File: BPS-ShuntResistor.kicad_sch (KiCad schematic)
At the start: 18 parts, among them J3 Amp_Conn

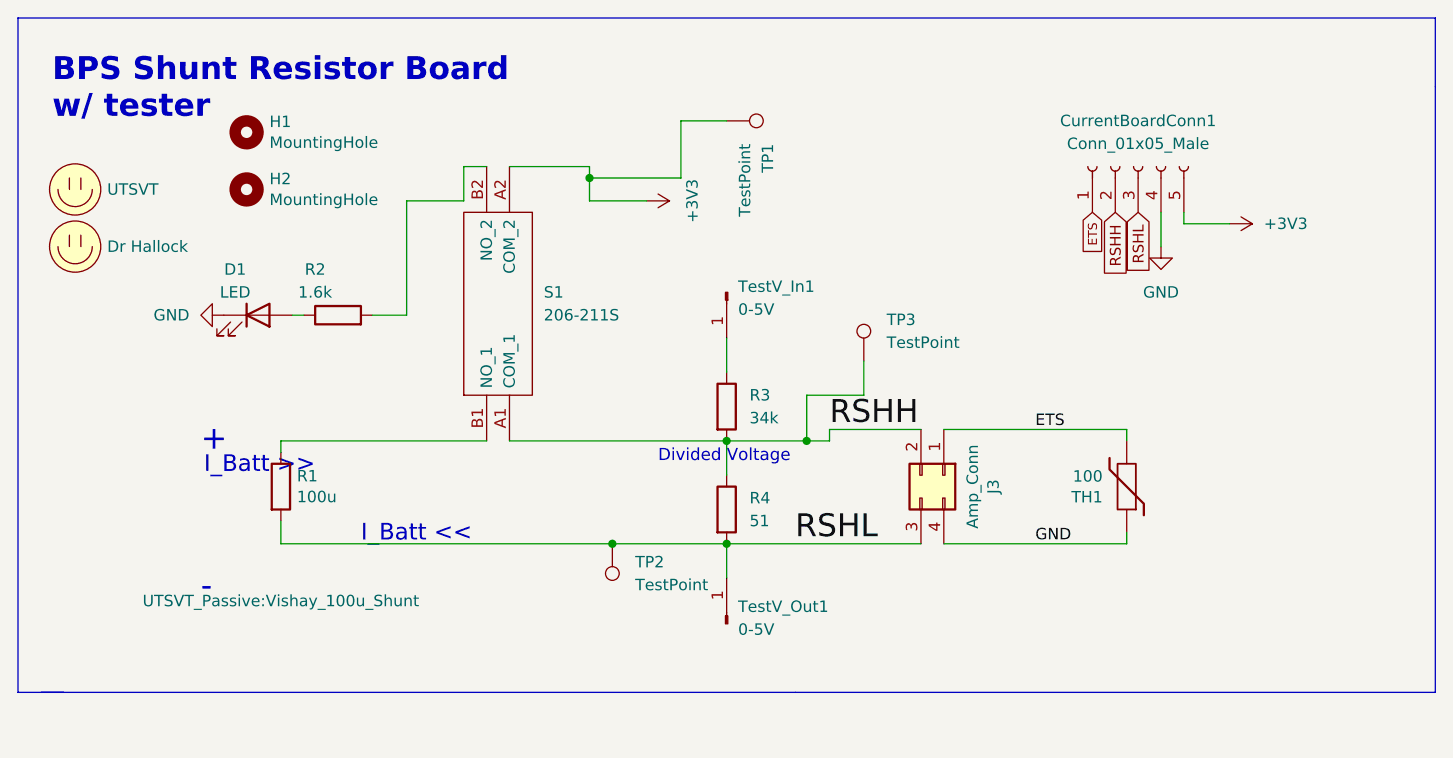
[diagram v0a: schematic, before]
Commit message: reorganizing board
workign on sync between amp board and this one
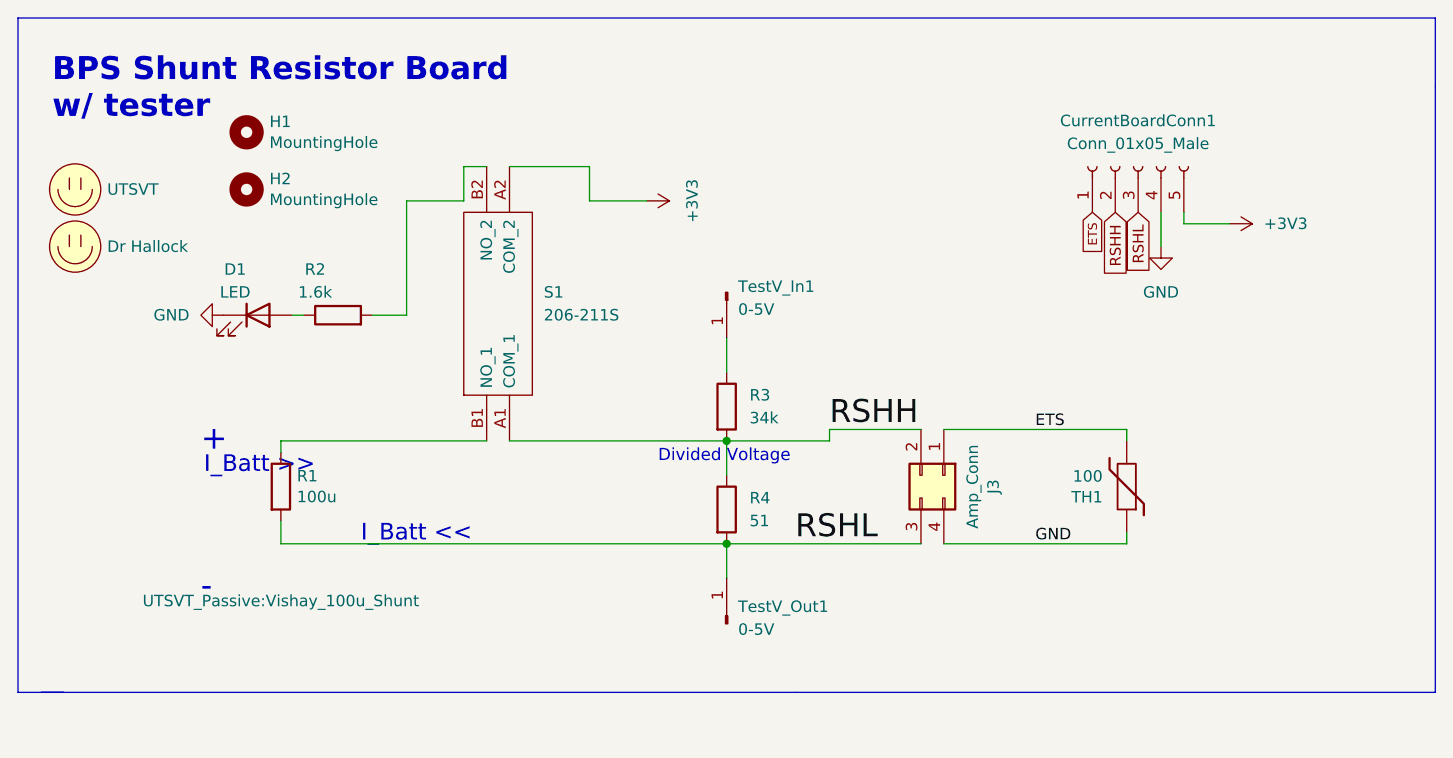
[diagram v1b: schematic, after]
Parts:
- removed TP1, TP2, TP3: TestPoint, TestPoint:TestPoint_Keystone_5005-5009_Compact, symbol Connector:TestPoint
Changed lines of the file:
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@@
 (kicad_sch (version 20211123) (generator eeschema)
   (paper "A4")
-  (junction (at 140.97 118.11) (diameter 0) (color 0 0 0 0)
-  )
-  (junction (at 162.56 106.68) (diameter 0) (color 0 0 0 0)
-  )
-  (junction (at 138.43 77.47) (diameter 0) (color 0 0 0 0)
-  )
   (junction (at 153.67 106.68) (diameter 0) (color 0 0 0 0)
   )
@@
     (stroke (width 0) (type default) (color 0 0 0 0))
   )
-  (wire (pts (xy 153.67 106.68) (xy 162.56 106.68))
-    (stroke (width 0) (type default) (color 0 0 0 0))
-  )
-  (wire (pts (xy 140.97 118.11) (xy 153.67 118.11))
+  (wire (pts (xy 153.67 106.68) (xy 165.1 106.68))
     (stroke (width 0) (type default) (color 0 0 0 0))
   )
@@
     (stroke (width 0) (type default) (color 0 0 0 0))
   )
-  (wire (pts (xy 162.56 101.6) (xy 162.56 106.68))
-    (stroke (width 0) (type default) (color 0 0 0 0))
-  )
   (wire (pts (xy 104.14 106.68) (xy 104.14 107.95))
     (stroke (width 0) (type default) (color 0 0 0 0))
@@
     (stroke (width 0) (type default) (color 0 0 0 0))
   )
-  (wire (pts (xy 148.59 71.12) (xy 148.59 77.47))
-    (stroke (width 0) (type default) (color 0 0 0 0))
-  )
   (wire (pts (xy 153.67 118.11) (xy 153.67 121.92))
     (stroke (width 0) (type default) (color 0 0 0 0))
   )
-  (wire (pts (xy 148.59 77.47) (xy 138.43 77.47))
-    (stroke (width 0) (type default) (color 0 0 0 0))
-  )
   (wire (pts (xy 124.46 80.01) (xy 124.46 76.2))
     (stroke (width 0) (type default) (color 0 0 0 0))
@@
     (stroke (width 0) (type default) (color 0 0 0 0))
   )
-  (wire (pts (xy 138.43 77.47) (xy 138.43 80.01))
+  (wire (pts (xy 138.43 76.2) (xy 138.43 80.01))
     (stroke (width 0) (type default) (color 0 0 0 0))
   )
@@
     (stroke (width 0) (type default) (color 0 0 0 0))
   )
-  (wire (pts (xy 153.67 71.12) (xy 148.59 71.12))
-    (stroke (width 0) (type default) (color 0 0 0 0))
-  )
-  (wire (pts (xy 168.91 101.6) (xy 162.56 101.6))
-    (stroke (width 0) (type default) (color 0 0 0 0))
-  )
   (wire (pts (xy 114.3 92.71) (xy 118.11 92.71))
     (stroke (width 0) (type default) (color 0 0 0 0))
   )
-  (wire (pts (xy 104.14 118.11) (xy 140.97 118.11))
+  (wire (pts (xy 104.14 118.11) (xy 153.67 118.11))
     (stroke (width 0) (type default) (color 0 0 0 0))
   )
@@
     (stroke (width 0) (type default) (color 0 0 0 0))
   )
-  (wire (pts (xy 138.43 76.2) (xy 138.43 77.47))
-    (stroke (width 0) (type default) (color 0 0 0 0))
-  )
   (wire (pts (xy 105.41 92.71) (xy 106.68 92.71))
     (stroke (width 0) (type default) (color 0 0 0 0))
   )
   (wire (pts (xy 153.67 106.68) (xy 153.67 110.49))
-    (stroke (width 0) (type default) (color 0 0 0 0))
-  )
-  (wire (pts (xy 168.91 97.79) (xy 168.91 101.6))
-    (stroke (width 0) (type default) (color 0 0 0 0))
-  )
-  (wire (pts (xy 162.56 106.68) (xy 165.1 106.68))
     (stroke (width 0) (type default) (color 0 0 0 0))
   )
@@
     (pin "1")
   )
-  (symbol (lib_id "Connector:TestPoint") (at 168.91 97.79 0) (unit 1)
-    (in_bom yes) (on_board yes) (fields_autoplaced)
-    (property "Reference" "TP3" (id 0) (at 171.45 93.2179 0)
-      (effects (font (size 1.27 1.27)) (justify left))
-    )
-    (property "Value" "TestPoint" (id 1) (at 171.45 95.7579 0)
-      (effects (font (size 1.27 1.27)) (justify left))
-    )
-    (property "Footprint" "TestPoint:TestPoint_Keystone_5005-5009_Compact" (id 2) (at 173.99 97.79 0)
-      (effects (font (size 1.27 1.27)) hide)
-    )
-    (property "Datasheet" "~" (id 3) (at 173.99 97.79 0)
-      (effects (font (size 1.27 1.27)) hide)
-    )
-    (pin "1")
-  )
   (symbol (lib_id "Connector:Conn_01x01_Male") (at 153.67 90.17 270) (unit 1)
     (in_bom yes) (on_board yes) (fields_autoplaced)
@@
     )
     (property "Datasheet" "" (id 3) (at 209.55 82.55 0)
-      (effects (font (size 1.27 1.27)) hide)
-    )
-    (pin "1")
-  )
-  (symbol (lib_id "Connector:TestPoint") (at 153.67 71.12 270) (unit 1)
-    (in_bom yes) (on_board yes) (fields_autoplaced)
-    (property "Reference" "TP1" (id 0) (at 158.2421 73.66 0)
-      (effects (font (size 1.27 1.27)) (justify left))
-    )
-    (property "Value" "TestPoint" (id 1) (at 155.7021 73.66 0)
-      (effects (font (size 1.27 1.27)) (justify left))
-    )
-    (property "Footprint" "TestPoint:TestPoint_Keystone_5005-5009_Compact" (id 2) (at 153.67 76.2 0)
-      (effects (font (size 1.27 1.27)) hide)
-    )
-    (property "Datasheet" "~" (id 3) (at 153.67 76.2 0)
-      (effects (font (size 1.27 1.27)) hide)
-    )
-    (pin "1")
-  )
-  (symbol (lib_id "Connector:TestPoint") (at 140.97 118.11 180) (unit 1)
-    (in_bom yes) (on_board yes) (fields_autoplaced)
-    (property "Reference" "TP2" (id 0) (at 143.51 120.1419 0)
-      (effects (font (size 1.27 1.27)) (justify right))
-    )
-    (property "Value" "TestPoint" (id 1) (at 143.51 122.6819 0)
-      (effects (font (size 1.27 1.27)) (justify right))
-    )
-    (property "Footprint" "TestPoint:TestPoint_Keystone_5005-5009_Compact" (id 2) (at 135.89 118.11 0)
-      (effects (font (size 1.27 1.27)) hide)
-    )
-    (property "Datasheet" "~" (id 3) (at 135.89 118.11 0)
       (effects (font (size 1.27 1.27)) hide)
     )
@@
       (reference "TH1") (unit 1) (value "100") (footprint "Resistor_SMD:R_0805_2012Metric")
     )
-    (path "/a2c0827d-27e7-459e-b74e-82b71d0bcf7d"
-      (reference "TP1") (unit 1) (value "TestPoint") (footprint "TestPoint:TestPoint_Keystone_5005-5009_Compact")
-    )
-    (path "/a52bbaf7-274f-407b-9c3b-8b7919792ae5"
-      (reference "TP2") (unit 1) (value "TestPoint") (footprint "TestPoint:TestPoint_Keystone_5005-5009_Compact")
-    )
-    (path "/6f9c746a-56ac-4c76-a21a-897a0cead77e"
-      (reference "TP3") (unit 1) (value "TestPoint") (footprint "TestPoint:TestPoint_Keystone_5005-5009_Compact")
-    )
     (path "/84a7fc7b-5bd9-45c8-89b5-3a5bcad31a54"

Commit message: working on rework
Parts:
- removed D1: LED, LED_SMD:LED_0805_2012Metric, symbol Device:LED
- removed R2: 1.6k, Resistor_SMD:R_0805_2012Metric, symbol Device:R
- removed S1: 206-211S, custom footprints:206211S, symbol custom_reqs:206-211S
- removed TestV_In1, TestV_Out1: 0-5V, Connector_PinHeader_2.54mm:PinHeader_1x01_P2.54mm_Vertical, symbol Connector:Conn_01x01_Male
- added ShuntTestJumper: Conn_01x05_Male, Connector_PinHeader_2.54mm:PinHeader_1x05_P2.54mm_Vertical, symbol Connector:Conn_01x05_Female
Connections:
- net RSHH: now also ShuntTestJumper.3 (Pin_3)
- net RSHL: now also ShuntTestJumper.5 (Pin_5)
- net at R1.1: now also ShuntTestJumper.2 (Pin_2)
- net TestIn: now reaches R3.1
- net TestIn: now also ShuntTestJumper.4 (Pin_4)
- no-connect marks 0 -> 1

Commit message: fixing sch
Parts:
- renumbered ShuntTestJumper to ShuntTestJumper1
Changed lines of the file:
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@@
   (symbol (lib_id "Connector:Conn_01x05_Female") (at 128.27 91.44 90) (unit 1)
     (in_bom yes) (on_board yes) (fields_autoplaced)
-    (property "Reference" "ShuntTestJumper" (id 0) (at 128.27 86.36 90))
+    (property "Reference" "ShuntTestJumper1" (id 0) (at 128.27 86.36 90))
     (property "Value" "Conn_01x05_Male" (id 1) (at 128.27 88.9 90))
     (property "Footprint" "Connector_PinHeader_2.54mm:PinHeader_1x05_P2.54mm_Vertical" (id 2) (at 128.27 91.44 0)
@@
     )
     (path "/46651b6a-aae7-4589-85a3-9dbcf0861909"
-      (reference "ShuntTestJumper") (unit 1) (value "Conn_01x05_Male") (footprint "Connector_PinHeader_2.54mm:PinHeader_1x05_P2.54mm_Vertical")
+      (reference "ShuntTestJumper1") (unit 1) (value "Conn_01x05_Male") (footprint "Connector_PinHeader_2.54mm:PinHeader_1x05_P2.54mm_Vertical")
     )
     (path "/bff0be5b-fcea-4d1b-a22e-58c65723f733"

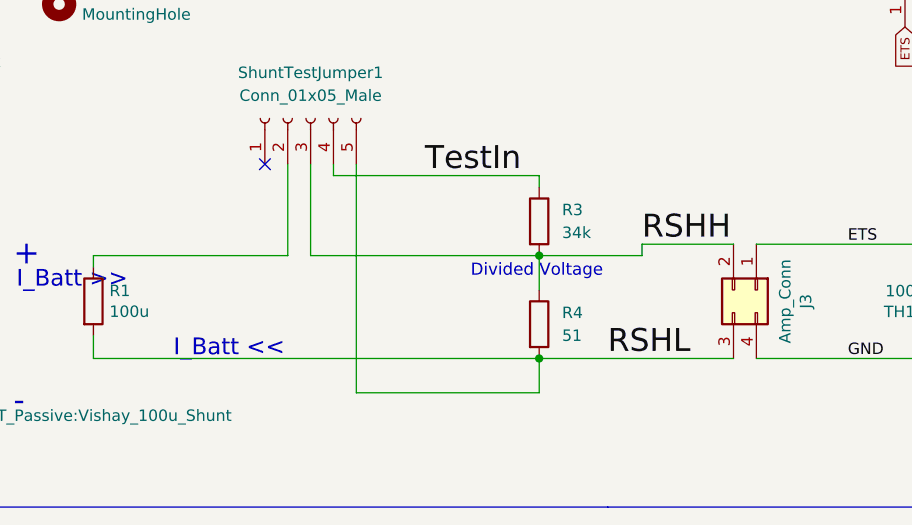
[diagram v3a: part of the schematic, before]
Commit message: Fixed RSHL/RSHH connectors
Net labels were in wrong spot on circuit
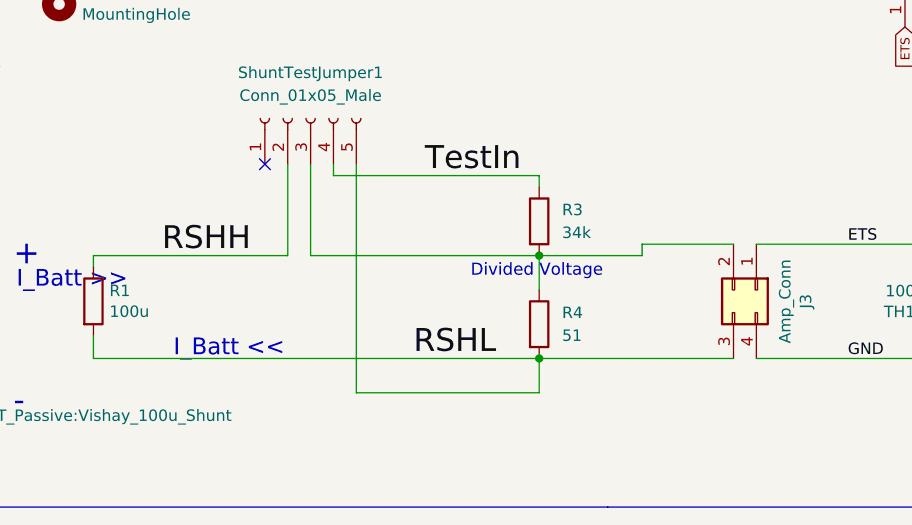
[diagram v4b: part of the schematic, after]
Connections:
- net RSHH: now also R1.1, ShuntTestJumper1.2 (Pin_2); no longer J3.2 (Pin_2), R3.2, R4.1, ShuntTestJumper1.3 (Pin_3)
- new net: J3.2 (Pin_2), R3.2, R4.1, ShuntTestJumper1.3 (Pin_3)
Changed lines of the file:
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@@
     (effects (font (size 1.27 1.27)) (justify left bottom))
   )
-  (label "RSHL" (at 161.29 118.11 0)
+  (label "RSHL" (at 139.7 118.11 0)
     (effects (font (size 2.54 2.54)) (justify left bottom))
   )
@@
     (effects (font (size 1.27 1.27)) (justify left bottom))
   )
-  (label "RSHH" (at 165.1 105.41 0)
+  (label "RSHH" (at 111.76 106.68 0)
     (effects (font (size 2.54 2.54)) (justify left bottom))
   )

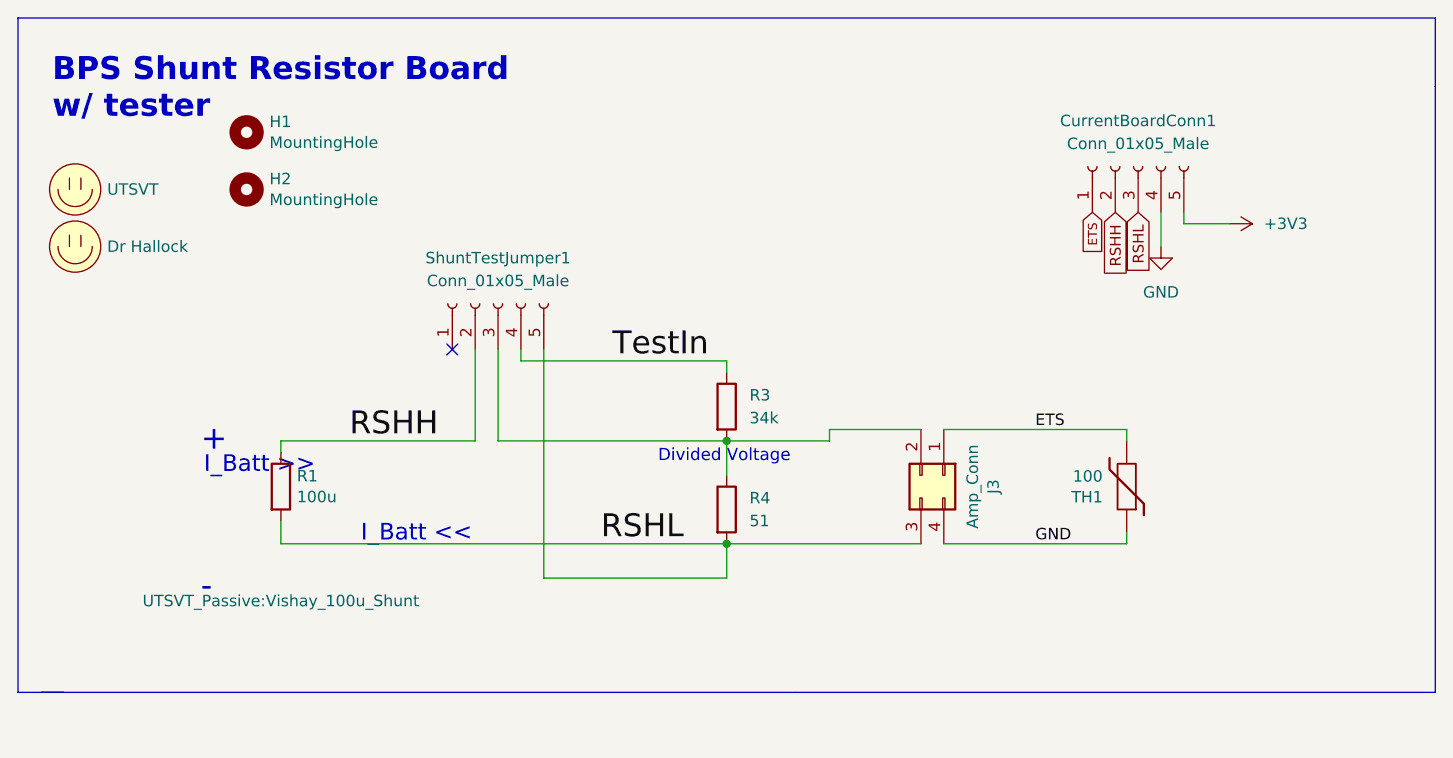
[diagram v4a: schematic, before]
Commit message: moved to exact same positions as tianda
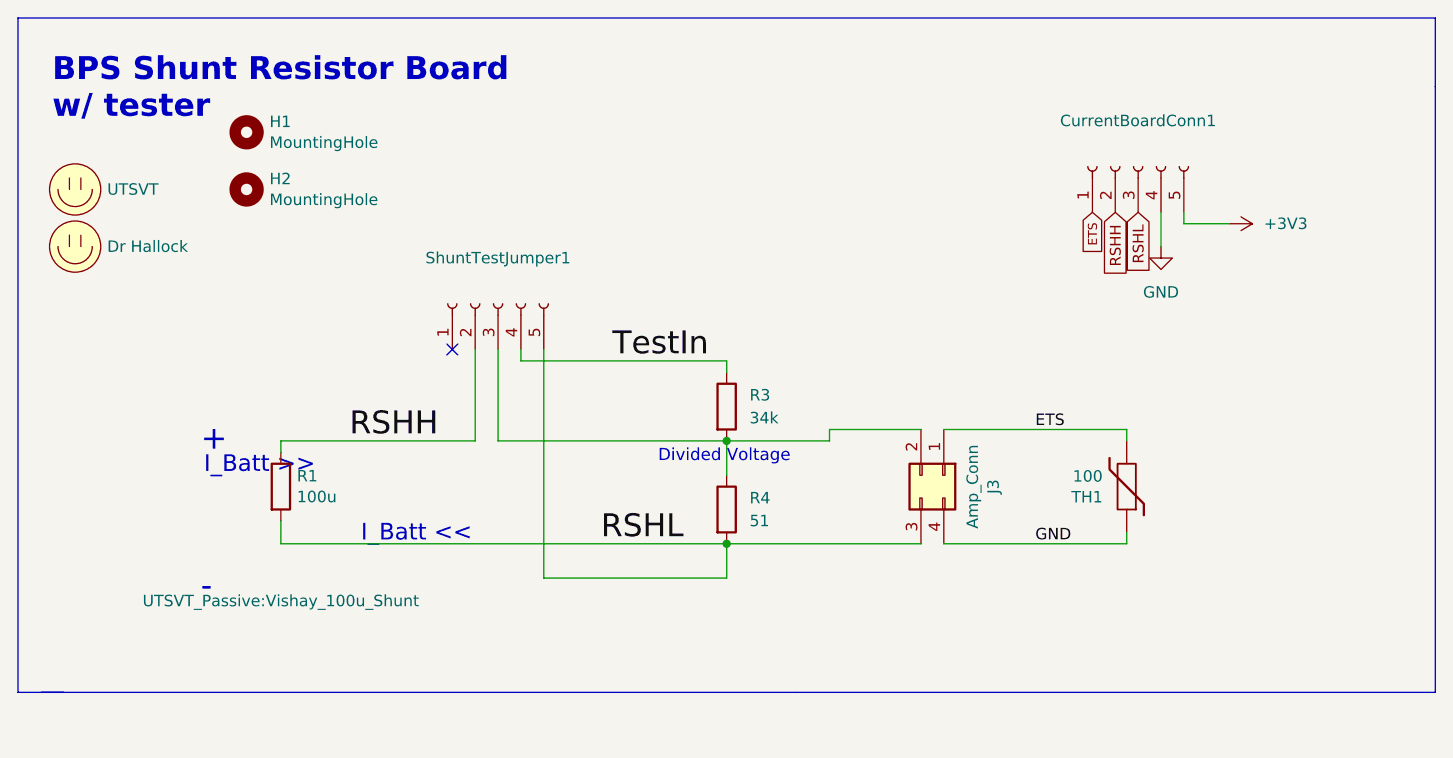
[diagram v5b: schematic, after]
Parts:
- CurrentBoardConn1, ShuntTestJumper1: value Conn_01x05_Male -> (none); footprint Connector_PinHeader_2.54mm:PinHeader_1x05_P2.54mm_Vertical -> (none)
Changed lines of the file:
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@@
     (in_bom yes) (on_board yes) (fields_autoplaced)
     (property "Reference" "ShuntTestJumper1" (id 0) (at 128.27 86.36 90))
-    (property "Value" "Conn_01x05_Male" (id 1) (at 128.27 88.9 90))
-    (property "Footprint" "Connector_PinHeader_2.54mm:PinHeader_1x05_P2.54mm_Vertical" (id 2) (at 128.27 91.44 0)
+    (property "Value" "" (id 1) (at 128.27 88.9 90))
+    (property "Footprint" "" (id 2) (at 128.27 91.44 0)
       (effects (font (size 1.27 1.27)) hide)
     )
@@
     (in_bom yes) (on_board yes) (fields_autoplaced)
     (property "Reference" "CurrentBoardConn1" (id 0) (at 199.39 71.12 90))
-    (property "Value" "Conn_01x05_Male" (id 1) (at 199.39 73.66 90))
-    (property "Footprint" "Connector_PinHeader_2.54mm:PinHeader_1x05_P2.54mm_Vertical" (id 2) (at 199.39 76.2 0)
+    (property "Value" "" (id 1) (at 199.39 73.66 90))
+    (property "Footprint" "" (id 2) (at 199.39 76.2 0)
       (effects (font (size 1.27 1.27)) hide)
     )
@@
     )
     (path "/4f59afea-52a6-42ef-a827-b3f6d4652563"
-      (reference "CurrentBoardConn1") (unit 1) (value "Conn_01x05_Male") (footprint "Connector_PinHeader_2.54mm:PinHeader_1x05_P2.54mm_Vertical")
+      (reference "CurrentBoardConn1") (unit 1) (value "Conn_01x05_Male") (footprint "Connector_PinHeader_2.54mm:PinHeader_1x05_P2.54mm_Vertical_SMD_Pin1Left")
     )
     (path "/00000000-0000-0000-0000-00005f6f5e19"
@@
     )
     (path "/46651b6a-aae7-4589-85a3-9dbcf0861909"
-      (reference "ShuntTestJumper1") (unit 1) (value "Conn_01x05_Male") (footprint "Connector_PinHeader_2.54mm:PinHeader_1x05_P2.54mm_Vertical")
+      (reference "ShuntTestJumper1") (unit 1) (value "Conn_01x05_Male") (footprint "Connector_PinHeader_2.54mm:PinHeader_1x05_P2.54mm_Vertical_SMD_Pin1Left")
     )
     (path "/bff0be5b-fcea-4d1b-a22e-58c65723f733"
